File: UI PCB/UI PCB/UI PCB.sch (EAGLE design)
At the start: 23 parts, among them IC1 MCP23S17SP, IC2 MCP23S17SP, X1 JST-XH-02-PIN-ROUND-PAD, X2 JST-XH-02-PIN-ROUND-PAD, X3 JST-XH-02-PIN-ROUND-PAD, X4 JST-XH-02-PIN-ROUND-PAD, X5 JST-XH-05-PIN-ROUND-PAD, X6 JST-XH-05-PIN-ROUND-PAD, X7 JST-XH-05-PIN-ROUND-PAD, X8 JST-XH-05-PIN-ROUND-PAD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

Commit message: added descriptions for busses and sheets
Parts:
- removed PL1: (no value), con-harting-v:16VS
- removed SV1: (no value), con-lsta:FE15-1
- added C3, C4: (no value), rcl:C-EUC0805
- added U$1: 2514-6002UB, 2514-6002UB:2514-6002UB
- added X10: (no value), con-weidmueller-sl35:180G-15
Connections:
- removed net A0: IC1.A0, IC2.A0, PL1-5.S
- removed net A1: IC1.A1, IC2.A1, PL1-6.S
- removed net CLK: PL1-7.S
- removed net N$16: PL1-16.S
- new net N$1: U$1.1
- new net N$10: U$1.6
- new net N$11: U$1.8
- new net N$12: U$1.10
- new net N$13: U$1.12
- new net N$14: U$1.14
- new net N$2: U$1.3
- new net N$3: U$1.5
- new net N$4: U$1.7
- new net N$5: U$1.9
- new net N$6: U$1.11
- new net N$7: U$1.13
- new net N$8: U$1.2
- new net N$9: U$1.4
- net 3V3: now also C3.1, C4.1, IC2.A0, X10.14; no longer PL1-13.S, SV1.14
- net 5V: now also X10.15; no longer PL1-14.S, SV1.15
- net CS1: no longer PL1-10.S
- net CS2: no longer PL1-11.S
- net GND: now also C3.2, C4.2, IC1.A0, IC1.A1, IC1.A2, IC2.A1, IC2.A2, X10.13; no longer PL1-15.S, SV1.13
- net GPA0: now also X10.12; no longer SV1.12
- net GPA1: now also X10.11; no longer SV1.11
- net GPA2: now also X10.10; no longer SV1.10
- net GPA3: now also X10.9; no longer SV1.9
- net GPA4: now also X10.8; no longer SV1.8
- net GPA5: now also X10.7; no longer SV1.7
- net GPA6: now also X10.6; no longer SV1.6
- net GPA7: now also X10.5; no longer SV1.5
- net GPB4: now also X10.4; no longer SV1.4
- net GPB5: now also X10.3; no longer SV1.3
- net GPB6: now also X10.2; no longer SV1.2
- net GPB7: now also X10.1; no longer SV1.1
- net INTA1: no longer PL1-1.S
- net INTA2: no longer PL1-3.S
- net INTB1: no longer PL1-2.S
- net INTB2: no longer PL1-4.S
- net MISO: no longer PL1-8.S
- net MOSI: no longer PL1-9.S
- net RESET: no longer PL1-12.S

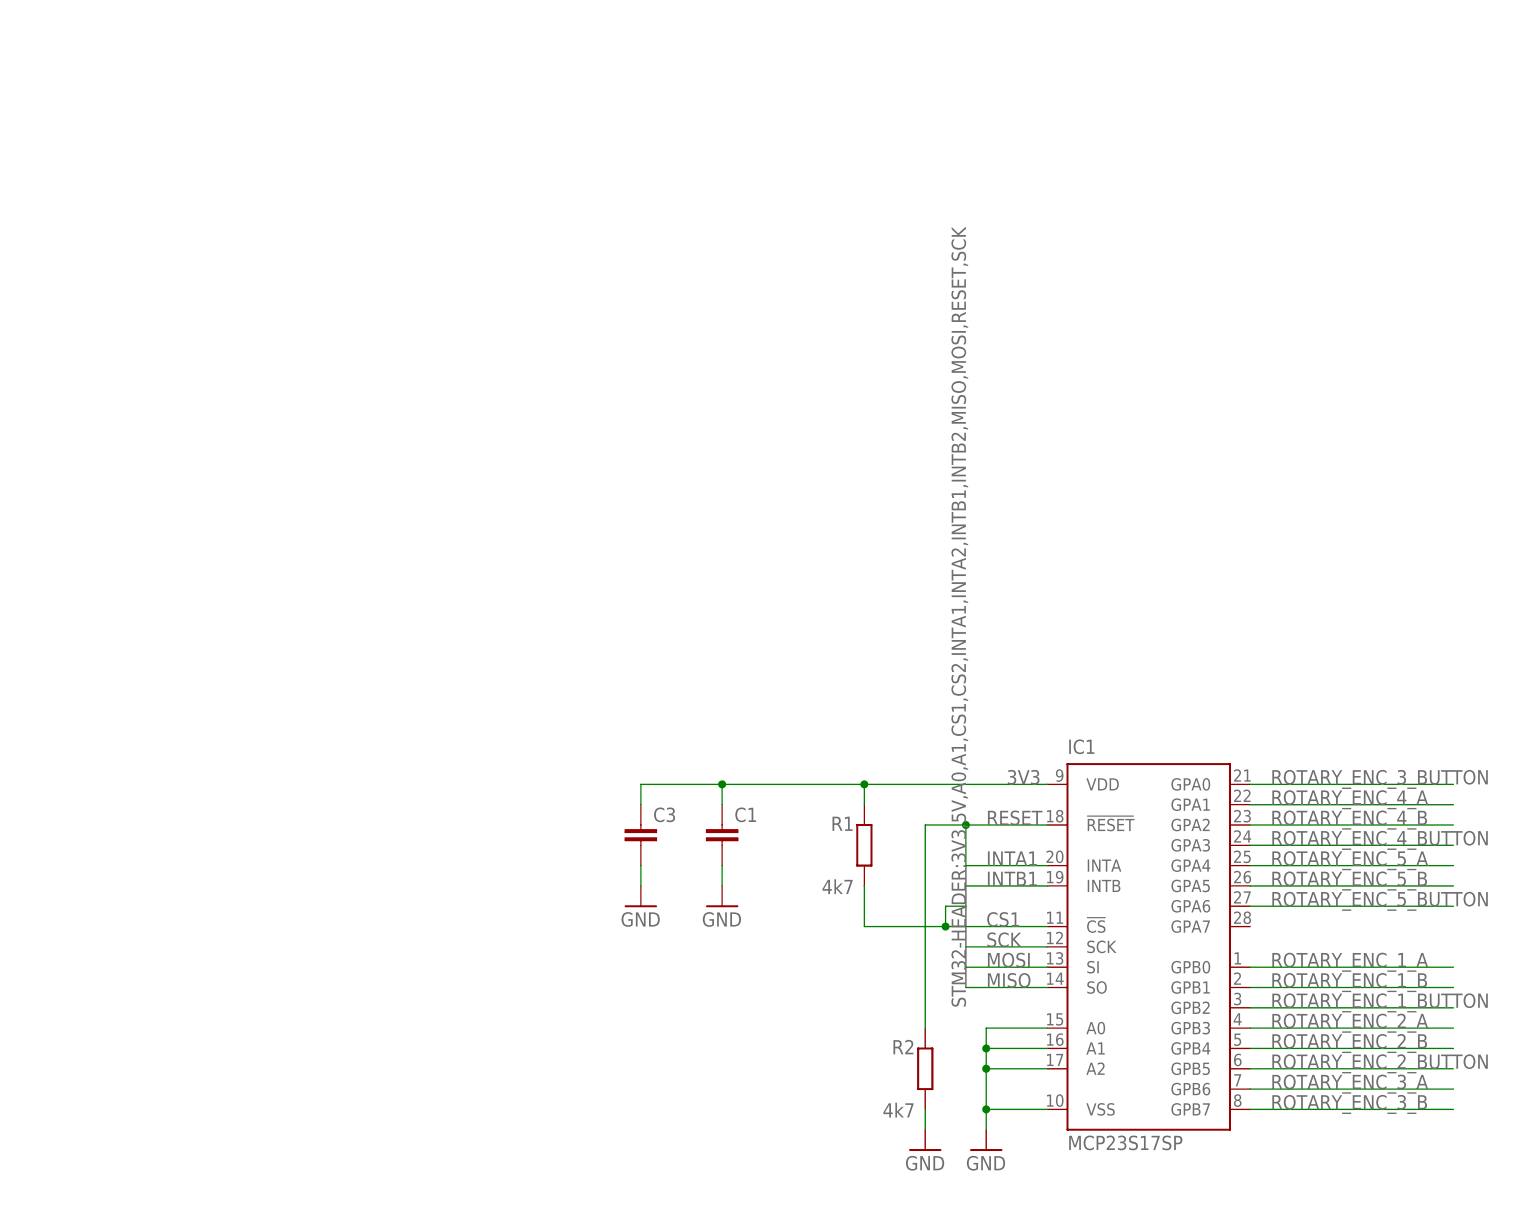
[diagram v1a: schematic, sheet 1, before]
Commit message: improve the schemetic on the io expanders and add the right header for the stm32 connection
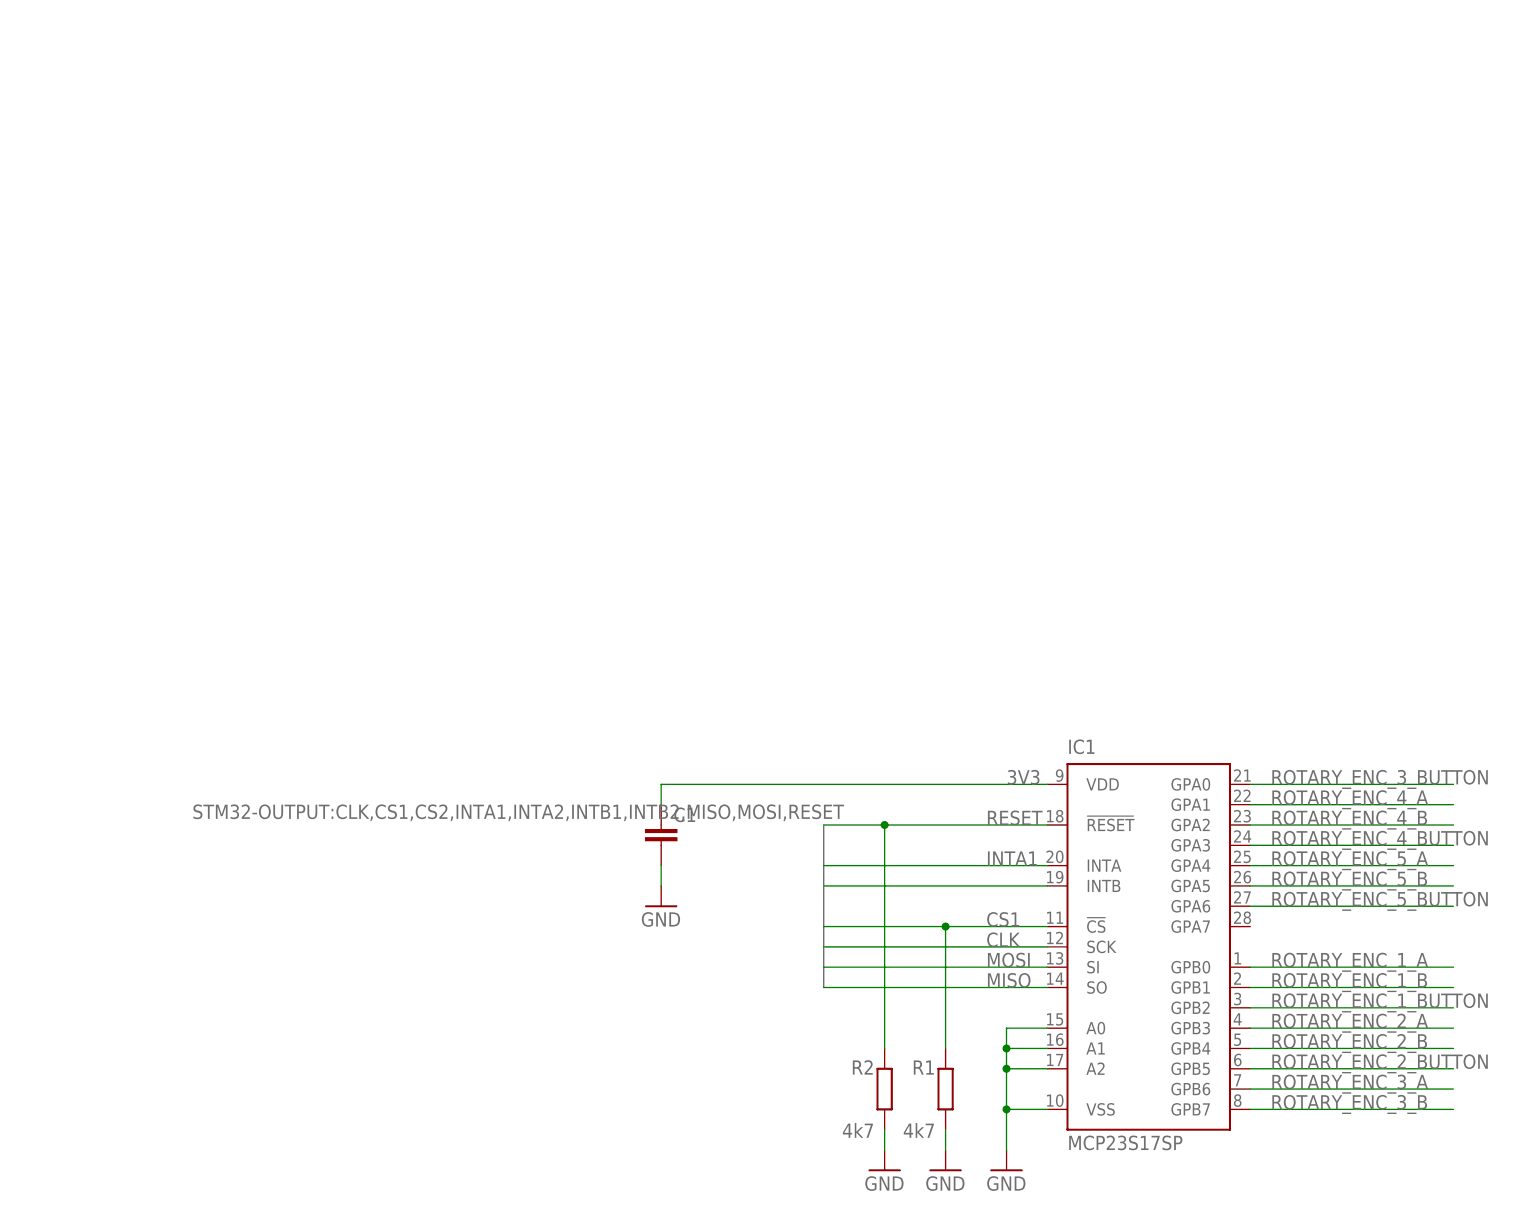
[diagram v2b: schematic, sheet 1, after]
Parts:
- removed C3, C4: (no value), rcl:C-EUC0805
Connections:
- net N$1 renamed OPEN
- removed net N$10: U$1.6
- removed net N$11: U$1.8
- removed net N$12: U$1.10
- removed net N$13: U$1.12
- removed net N$14: U$1.14
- removed net N$2: U$1.3
- removed net N$3: U$1.5
- removed net N$4: U$1.7
- removed net N$5: U$1.9
- removed net N$6: U$1.11
- removed net N$7: U$1.13
- removed net N$8: U$1.2
- removed net N$9: U$1.4
- removed net SCK: IC1.SCK, IC2.SCK
- new net CLK: IC1.SCK, IC2.SCK, U$1.14
- net 3V3: now also U$1.4; no longer C3.1, C4.1, R1.2, R3.2
- net 5V: now also U$1.3
- net CS1: now also R1.2, U$1.11; no longer R1.1
- net CS2: now also R3.2, U$1.10; no longer R3.1
- net GND: now also R1.1, R3.1, U$1.2; no longer C3.2, C4.2
- net INTA1: now also U$1.8
- net INTA2: now also U$1.5
- net INTB1: now also U$1.7
- net INTB2: now also U$1.6
- net MISO: now also U$1.13
- net MOSI: now also U$1.12
- net RESET: now also U$1.9
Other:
- moved on the sheet: C1, C2, R1, R2, R3, R4

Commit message: redesigned PCB
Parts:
- removed X10: (no value), con-weidmueller-sl35:180G-15
- added J1: (no value), SparkFun-Connectors:CONN_15
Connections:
- net 3V3: now also J1.14, X5-2.S, X6-2.S, X7-2.S, X8-2.S, X9-2.S; no longer X10.14, X5-3.S, X6-3.S, X7-3.S, X8-3.S, X9-3.S
- net 5V: now also J1.15; no longer X10.15
- net GND: now also J1.13, X5-1.S, X6-1.S, X7-1.S, X8-1.S, X9-1.S; no longer X10.13, X5-2.S, X6-2.S, X7-2.S, X8-2.S, X9-2.S
- net GPA0: now also J1.12; no longer X10.12
- net GPA1: now also J1.11; no longer X10.11
- net GPA2: now also J1.10; no longer X10.10
- net GPA3: now also J1.9; no longer X10.9
- net GPA4: now also J1.8; no longer X10.8
- net GPA5: now also J1.7; no longer X10.7
- net GPA6: now also J1.6; no longer X10.6
- net GPA7: now also J1.5; no longer X10.5
- net GPB4: now also J1.4; no longer X10.4
- net GPB5: now also J1.3; no longer X10.3
- net GPB6: now also J1.2; no longer X10.2
- net GPB7: now also J1.1; no longer X10.1
- net ROTARY_ENC_1_A: now also X5-5.S; no longer X5-1.S
- net ROTARY_ENC_1_B: now also X5-4.S; no longer X5-5.S
- net ROTARY_ENC_1_BUTTON: now also X5-3.S; no longer X5-4.S
- net ROTARY_ENC_2_A: now also X6-5.S; no longer X6-1.S
- net ROTARY_ENC_2_B: now also X6-4.S; no longer X6-5.S
- net ROTARY_ENC_2_BUTTON: now also X6-3.S; no longer X6-4.S
- net ROTARY_ENC_3_A: now also IC1.GPB7, X7-5.S; no longer IC1.GPB6, X7-1.S
- net ROTARY_ENC_3_B: now also IC1.GPB6, X7-4.S; no longer IC1.GPB7, X7-5.S
- net ROTARY_ENC_3_BUTTON: now also X7-3.S; no longer X7-4.S
- net ROTARY_ENC_4_A: now also X8-5.S; no longer X8-1.S
- net ROTARY_ENC_4_B: now also X8-4.S; no longer X8-5.S
- net ROTARY_ENC_4_BUTTON: now also X8-3.S; no longer X8-4.S
- net ROTARY_ENC_5_A: now also X9-5.S; no longer X9-1.S
- net ROTARY_ENC_5_B: now also X9-4.S; no longer X9-5.S
- net ROTARY_ENC_5_BUTTON: now also X9-3.S; no longer X9-4.S

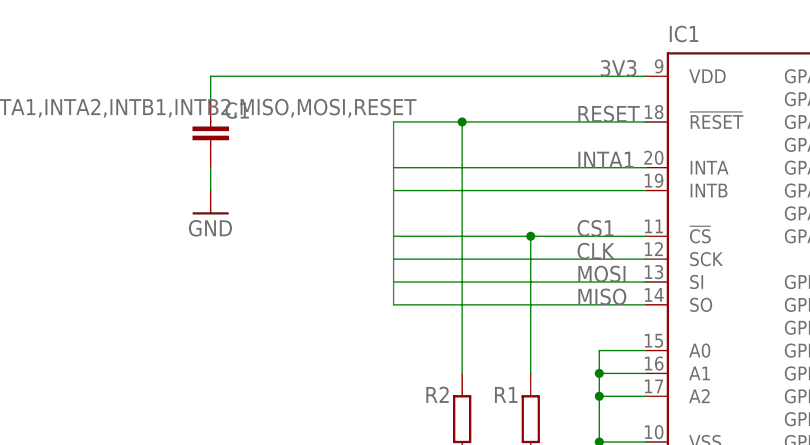
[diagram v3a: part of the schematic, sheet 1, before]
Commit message: some changes to PCB design, thicker power supply lines
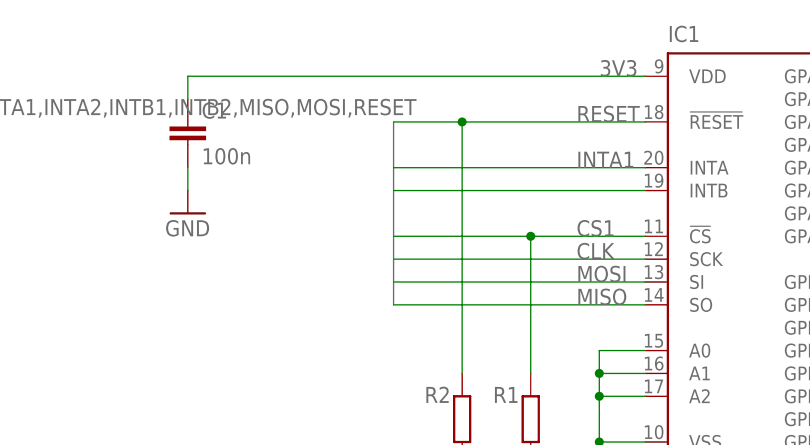
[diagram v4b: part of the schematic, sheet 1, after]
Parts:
- C1, C2: value (none) -> 100n; device rcl:C-EUC0805 -> rcl:C-EUC0603
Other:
- moved on the sheet: C1, C2
